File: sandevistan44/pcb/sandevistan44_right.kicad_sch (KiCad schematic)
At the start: 49 parts, among them J2 TRRS, SW23 SW_PUSH, SW24 SW_PUSH, SW25 SW_PUSH, SW26 SW_PUSH, SW27 SW_PUSH, SW28 SW_PUSH, SW29 SW_PUSH, SW30 SW_PUSH, SW31 SW_PUSH, SW32 SW_PUSH, SW33 SW_PUSH, SW34 SW_PUSH, SW35 SW_PUSH, SW36 SW_PUSH, SW37 SW_PUSH, SW38 SW_PUSH, SW39 SW_PUSH, SW40 SW_PUSH, SW41 SW_PUSH, SW42 SW_PUSH, SW43 SW_PUSH, SW44 SW_PUSH, U2 ProMicro

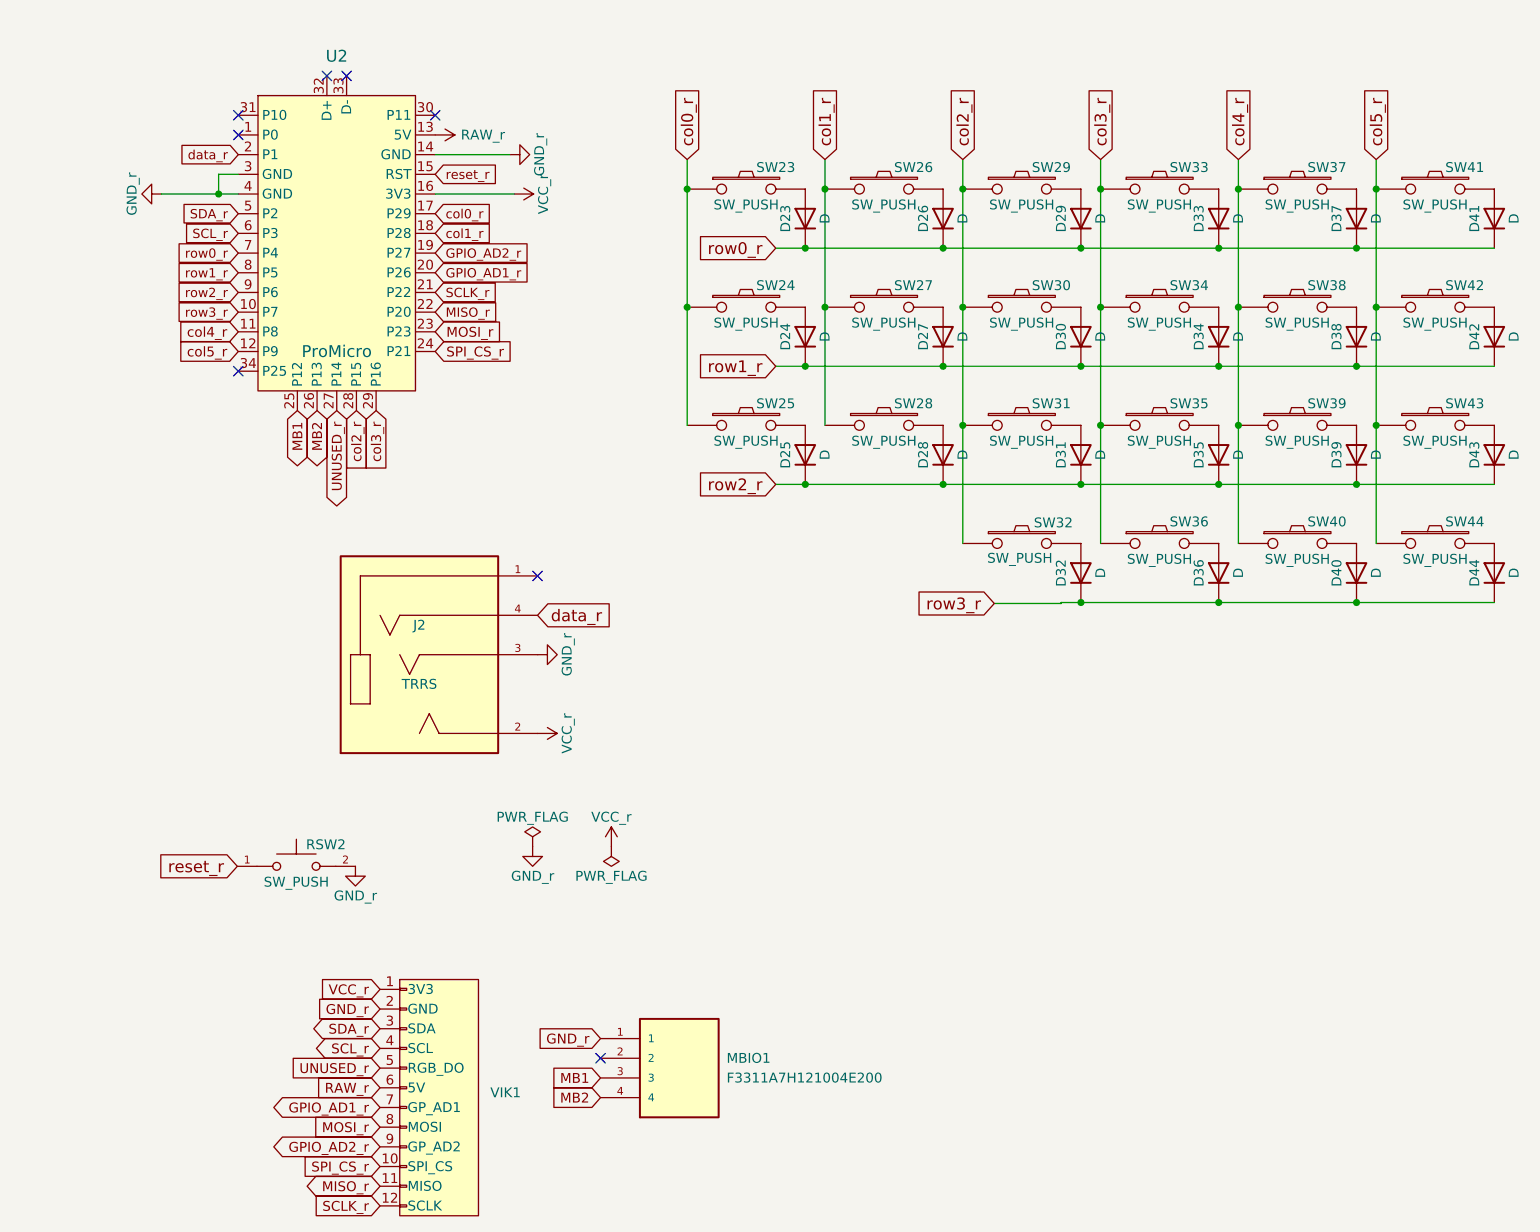
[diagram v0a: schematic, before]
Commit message: Finish first iteration of 0.2 configuration
- Add encoders on each side and add body extension
- Modify trackball module cutout to allow for up to 55mm trackball
- Rewire again to fit new layout
- Fix/cleanup footprints
- Rework standoff holes to fit with new switch footprints
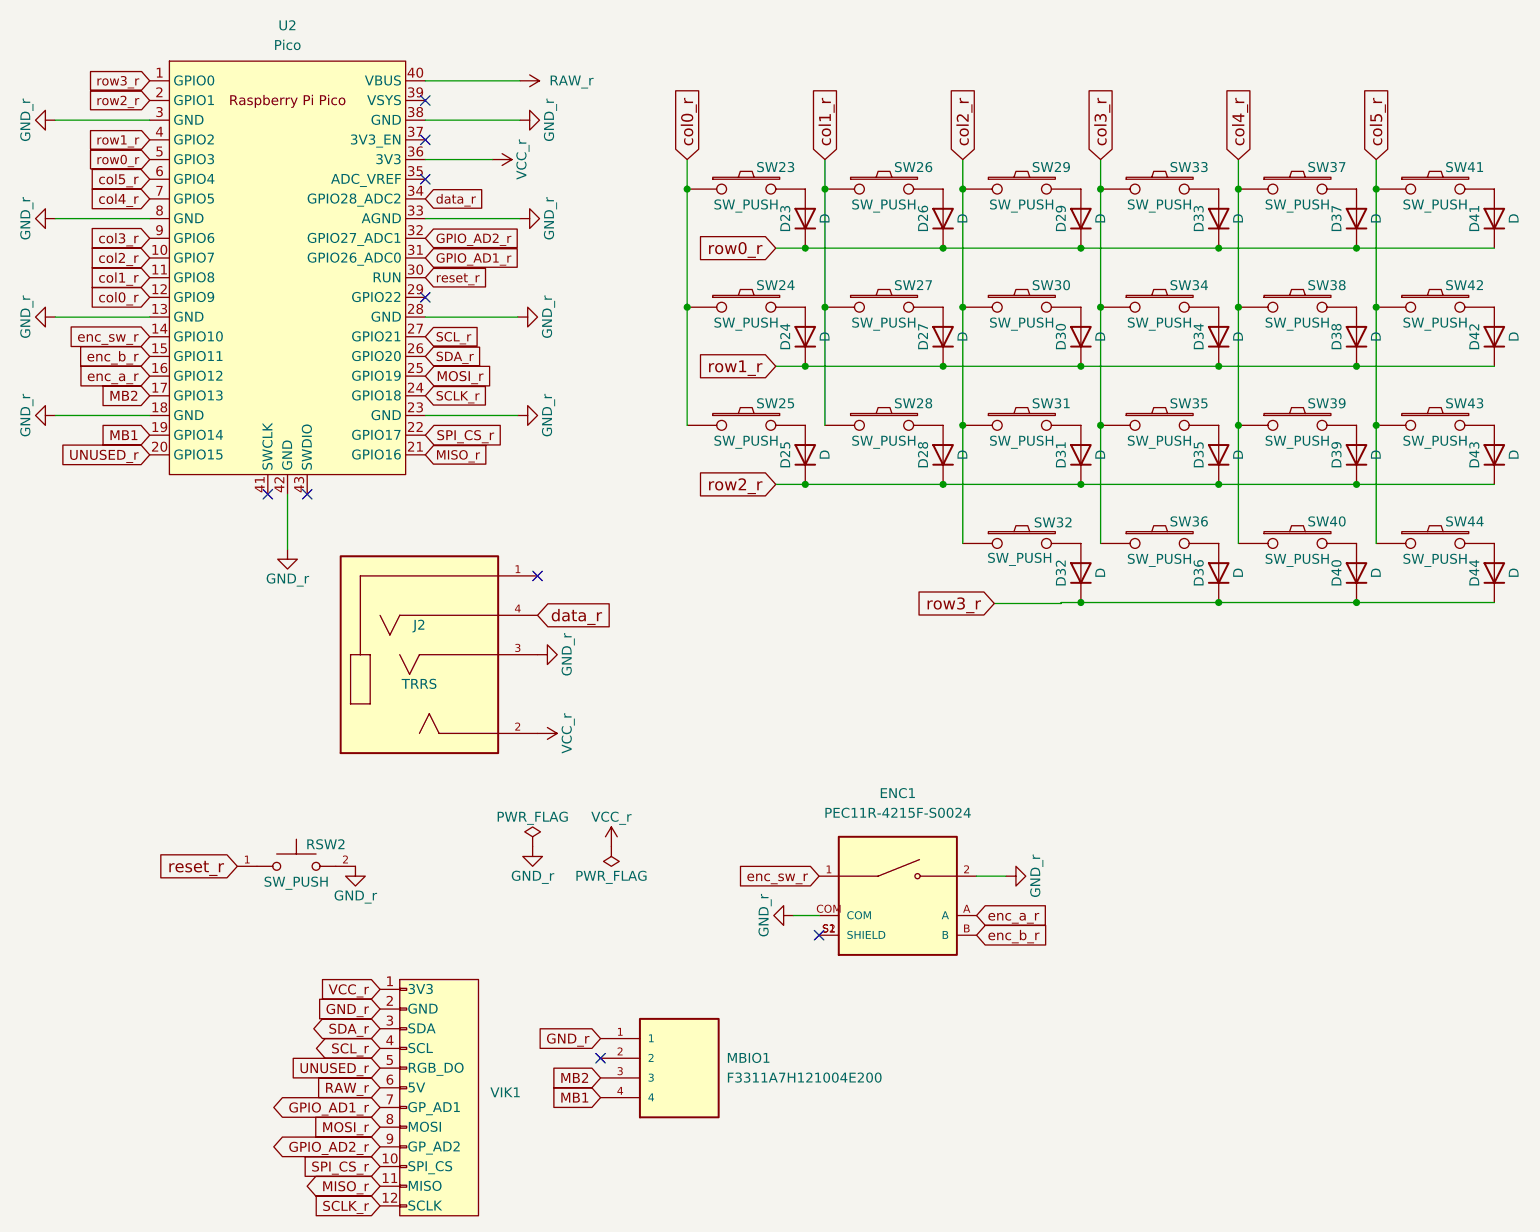
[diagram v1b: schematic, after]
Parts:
- removed U2: ProMicro, marbastlib-xp-promicroish:Helios_AC, symbol marbastlib-promicroish:Helios
- added ENC1: PEC11R-4215F-S0024, Library:XDCR_PEC11R-4215F-S0024, symbol PEC11R-4215F-S0024:PEC11R-4215F-S0024
- added U2: Pico, Library:RPi_Pico_SMD_TH_no_through_holes, symbol MCU_RaspberryPi_and_Boards:Pico
- SW23, SW24, SW25, SW26, SW27, SW28, SW29, SW30, SW31, SW32, SW33, SW34, SW35, SW36, SW37, SW38, SW39, SW40, SW41, SW42, SW43: footprint Library:SW_Hotswap_Kailh_Choc_V2_1.00u -> Library:Universal Switch Footprint (1u)
- SW44: footprint Library:SW_Hotswap_Kailh_Choc_V2_1.25u -> Library:Universal Switch Footprint (1.5u)
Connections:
- net GND_r: now also ENC1.2, ENC1.COM, U2.13 (GND), U2.18 (GND), U2.23 (GND), U2.28 (GND), U2.3 (GND), U2.33 (AGND), U2.38 (GND), U2.42 (GND), U2.8 (GND)
- net GPIO_AD1_r: now also U2.31 (GPIO26_ADC0)
- net GPIO_AD2_r: now also U2.32 (GPIO27_ADC1)
- net MB1: now also MBIO1.4, U2.19 (GPIO14); no longer MBIO1.3
- net MB2: now also MBIO1.3, U2.17 (GPIO13); no longer MBIO1.4
- net MISO_r: now also U2.21 (GPIO16)
- net MOSI_r: now also U2.25 (GPIO19)
- net RAW_r: now also U2.40 (VBUS)
- net SCLK_r: now also U2.24 (GPIO18)
- net SCL_r: now also U2.27 (GPIO21)
- net SDA_r: now also U2.26 (GPIO20)
- net SPI_CS_r: now also U2.22 (GPIO17)
- net UNUSED_r: now also U2.20 (GPIO15)
- net VCC_r: now also U2.36 (3V3)
- net col0_r: now also U2.12 (GPIO9)
- net col1_r: now also U2.11 (GPIO8)
- net col2_r: now also U2.10 (GPIO7)
- net col3_r: now also U2.9 (GPIO6)
- net col4_r: now also U2.7 (GPIO5)
- net col5_r: now also U2.6 (GPIO4)
- net data_r: now also U2.34 (GPIO28_ADC2)
- net reset_r: now also U2.30 (RUN)
- net row0_r: now also U2.5 (GPIO3)
- net row1_r: now also U2.4 (GPIO2)
- net row2_r: now also U2.2 (GPIO1)
- net row3_r: now also U2.1 (GPIO0)
- new net: ENC1.S1 (SHIELD), ENC1.S2 (SHIELD)
- new net enc_a_r: ENC1.A, U2.16 (GPIO12)
- new net enc_b_r: ENC1.B, U2.15 (GPIO11)
- new net enc_sw_r: ENC1.1, U2.14 (GPIO10)
- no-connect marks 8 -> 9

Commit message: Finalize left and right board setups
- Rework thumb cluster layout left and right
- Rework board shape on left and right
- Remove encoder from left side
- Rework wiring for better cleanliness/safety
- Reposition some standoff holes
- Move mouse button FFC connector
- Repin MCUs left and right for better routing
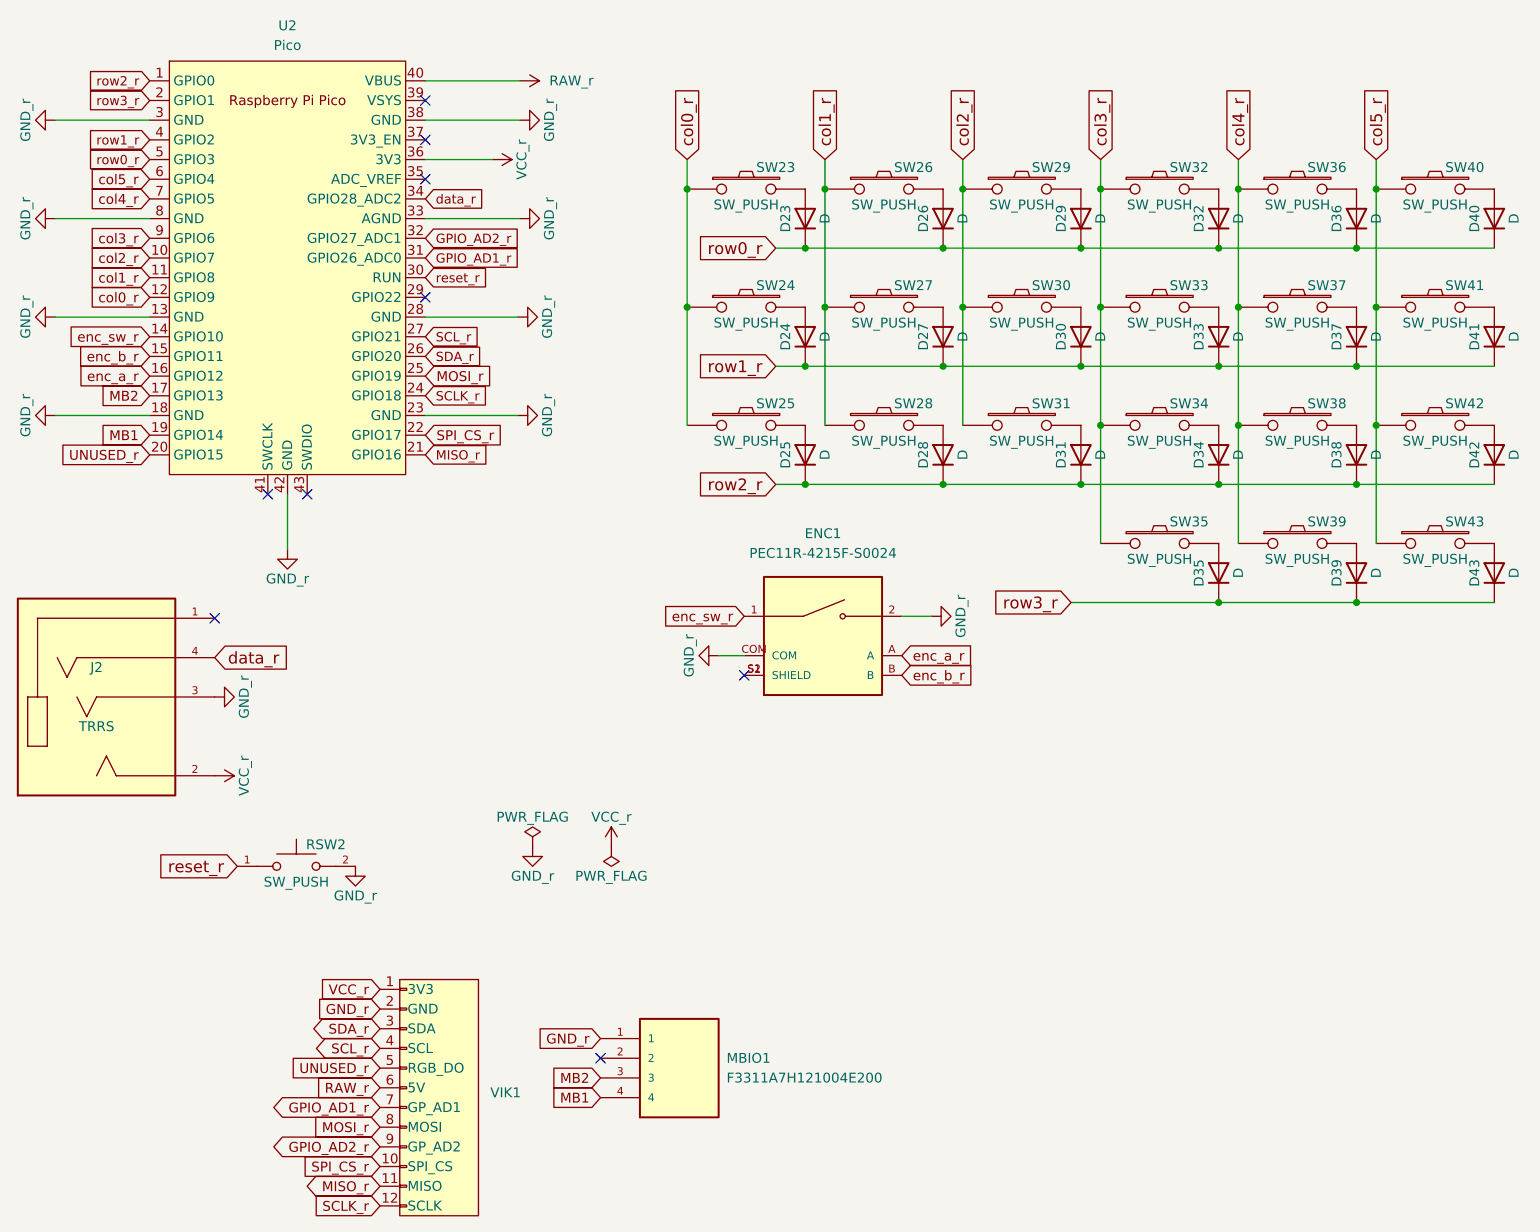
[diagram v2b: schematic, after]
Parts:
- removed D32: D, Library:TH 1N4148 Diode (long), symbol Device:D
- removed SW32: SW_PUSH, Library:Universal Switch Footprint (1u), symbol kbd:SW_PUSH
- ENC1: footprint Library:XDCR_PEC11R-4215F-S0024 -> Library:PEC11R_23mm_knob
- renumbered D33 to D32, D34 to D33, D35 to D34, D36 to D35, D37 to D36, D38 to D37, D39 to D38, D40 to D39, D41 to D40, D42 to D41, D43 to D42, D44 to D43, SW33 to SW32, SW34 to SW33, SW35 to SW34, SW36 to SW35, SW37 to SW36, SW38 to SW37, SW39 to SW38, SW40 to SW39, SW41 to SW40, SW42 to SW41, SW43 to SW42, SW44 to SW43
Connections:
- net row2_r: now also U2.1 (GPIO0); no longer U2.2 (GPIO1)
- net row3_r: now also U2.2 (GPIO1); no longer U2.1 (GPIO0)
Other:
- moved on the sheet: ENC1, J2
